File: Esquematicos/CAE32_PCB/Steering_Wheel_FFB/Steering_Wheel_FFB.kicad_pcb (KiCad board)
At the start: 2 copper layers, 145 x 145 mm, 4 parts

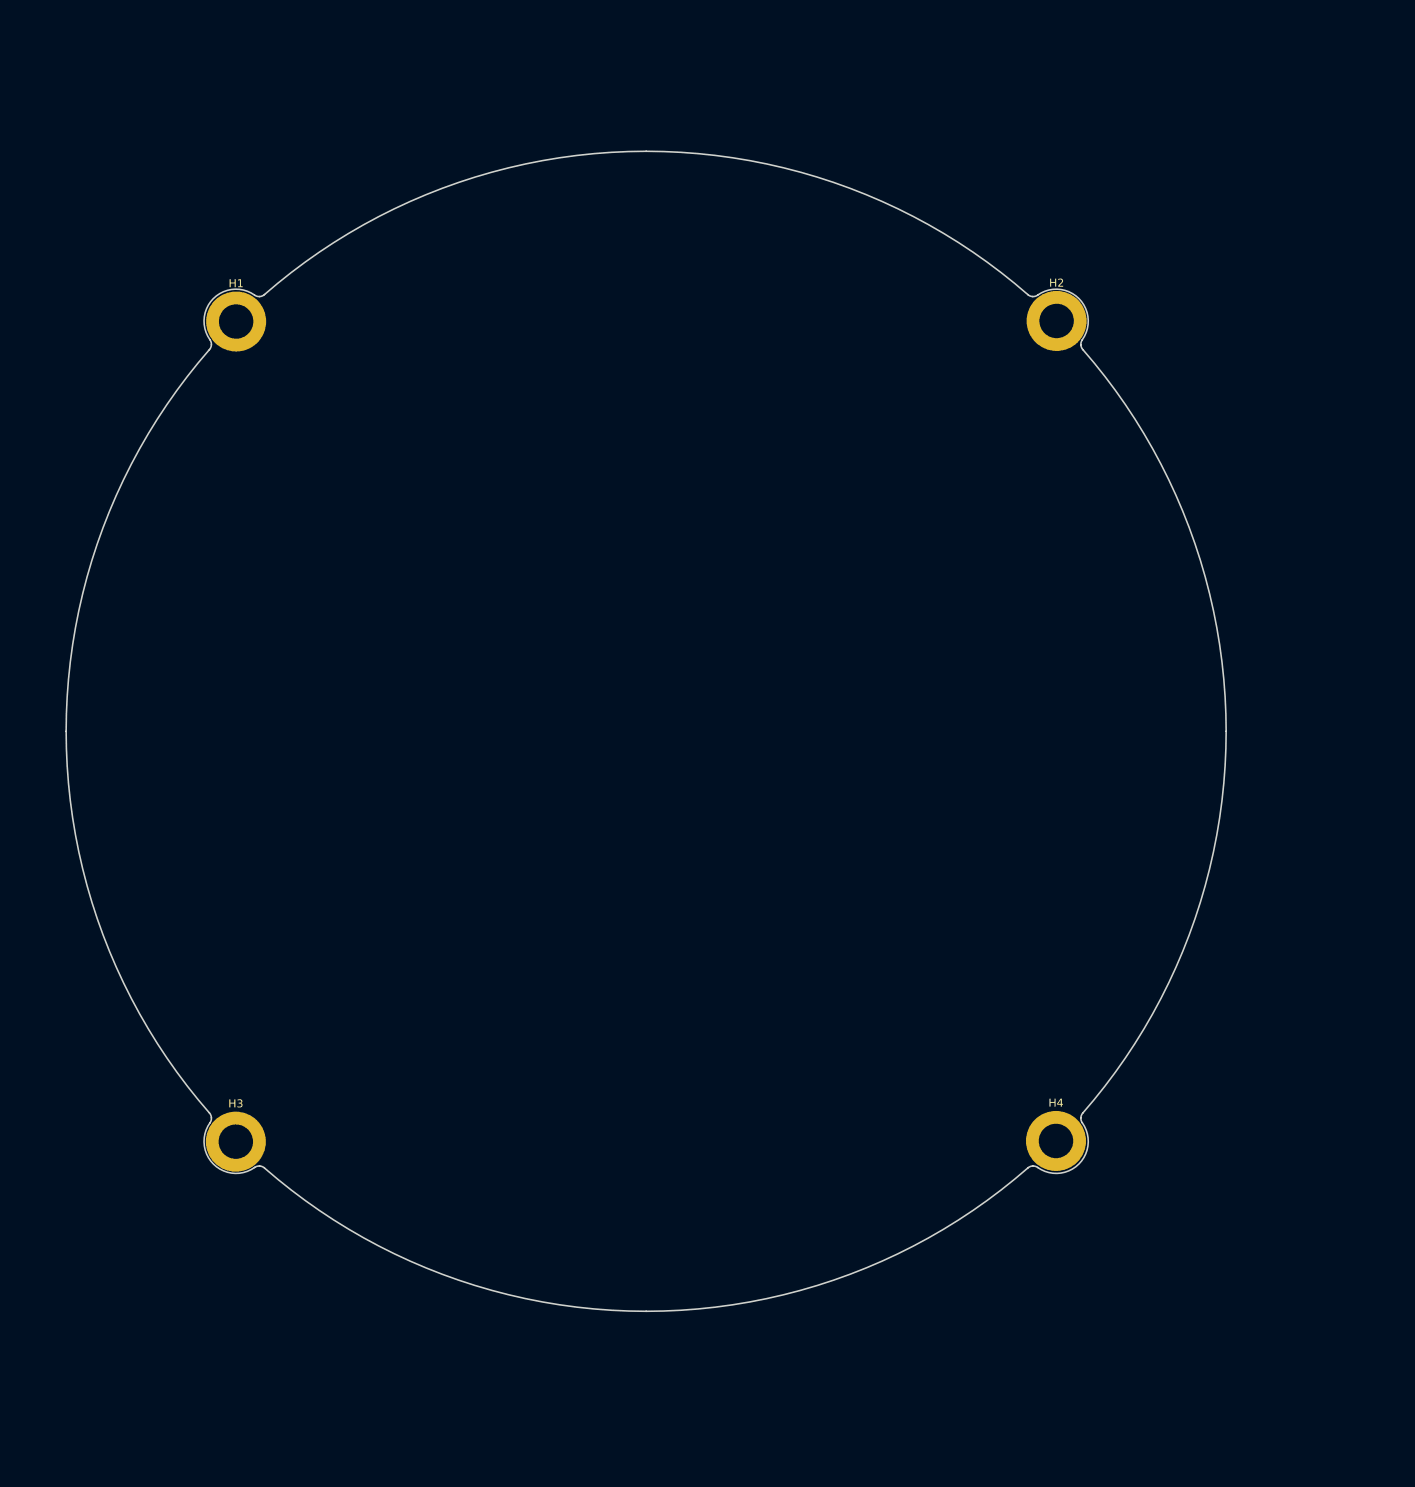
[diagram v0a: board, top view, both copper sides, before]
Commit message: update: change PCB for 2 layers to 4 layers
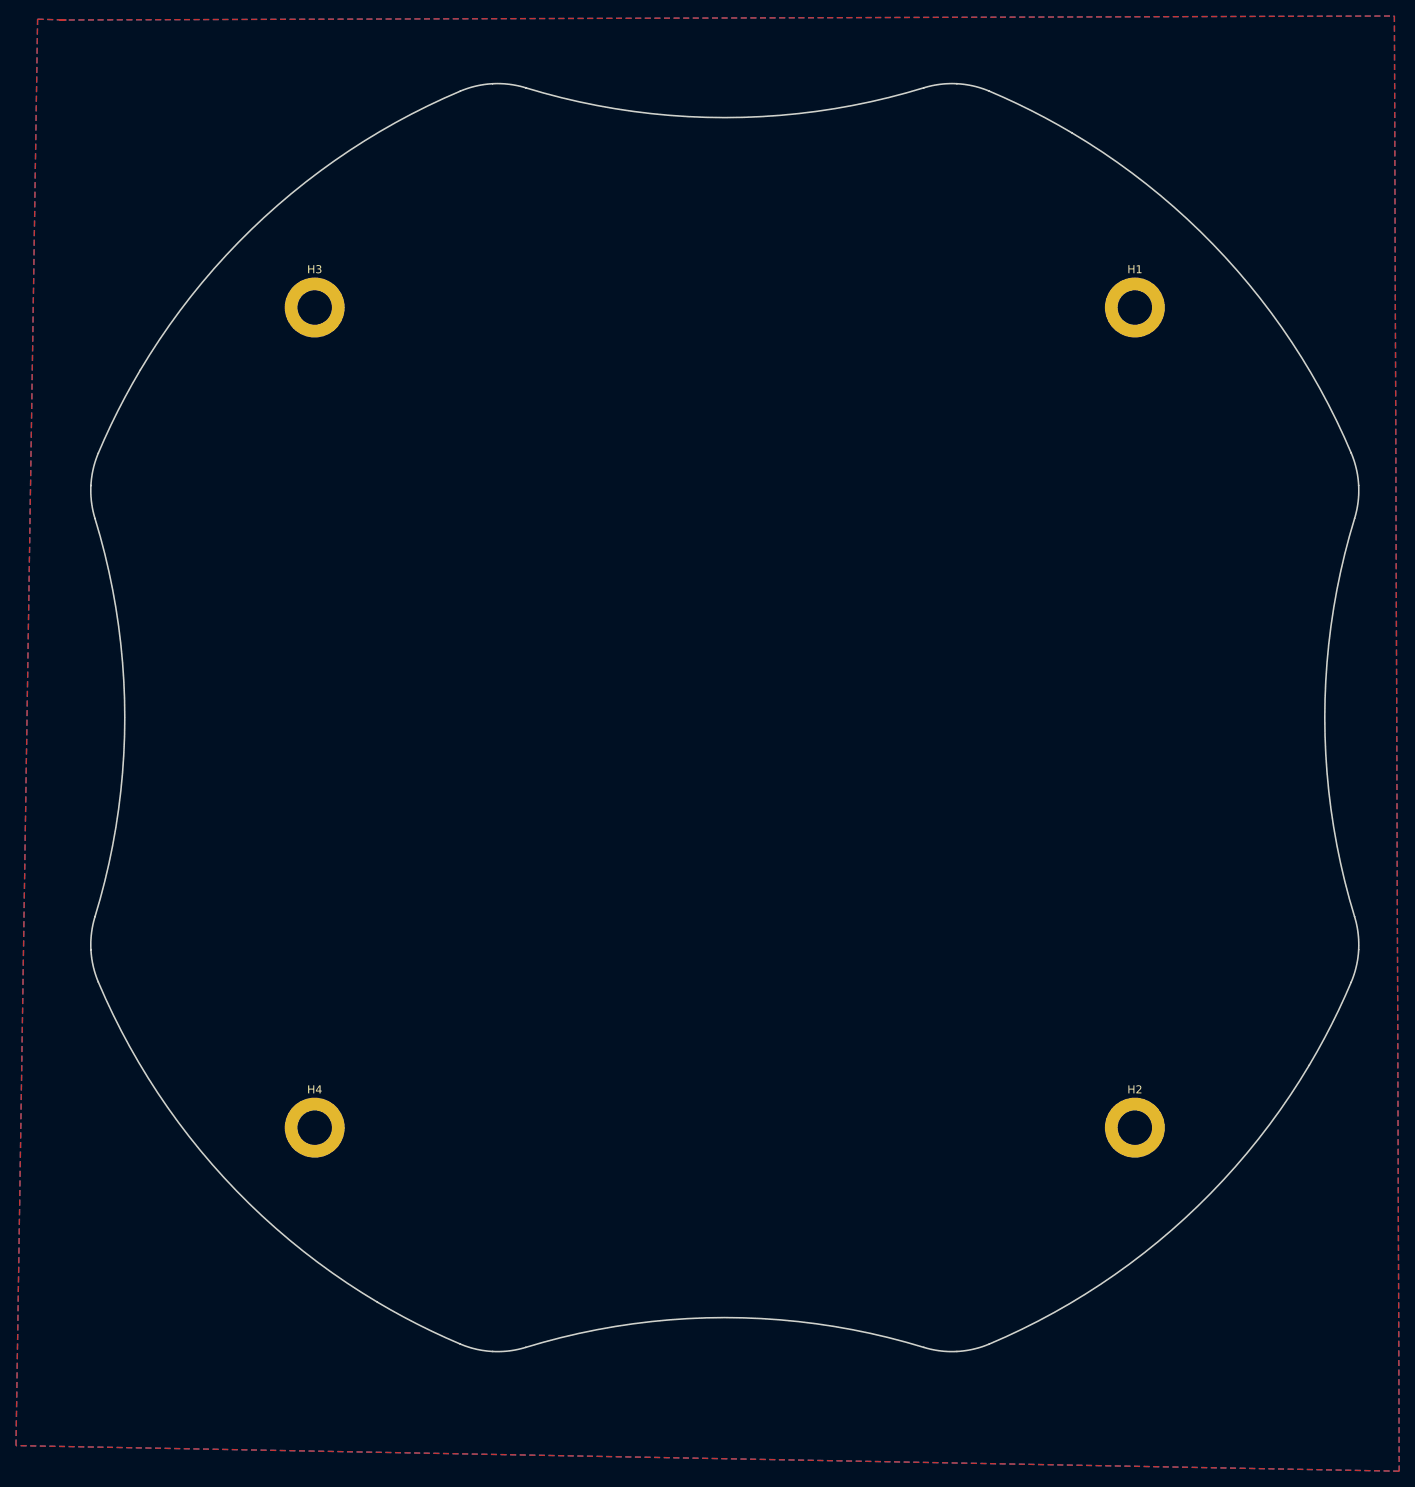
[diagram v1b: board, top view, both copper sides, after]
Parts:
- moved H1 112.4 mm to (165.3, 49.7)
- moved H3 104.7 mm to (62.7, 49.7)
- moved H2 101.3 mm to (165.3, 152.3)
- moved H4 92.7 mm to (62.7, 152.3)
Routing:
- added copper zone on B.Cu, net GNDREF
- added copper zone on F.Cu, net GNDREF
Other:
- board size 145 x 145 mm -> 158.5 x 158.5 mm
- copper layers 2 -> 4
